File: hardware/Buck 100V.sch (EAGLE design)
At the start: 26 parts, among them M1 SI3430DV, M2 SI5435BDC, Q1 FMMT625, Q2 FMMT723, U1 LT3756EMSE

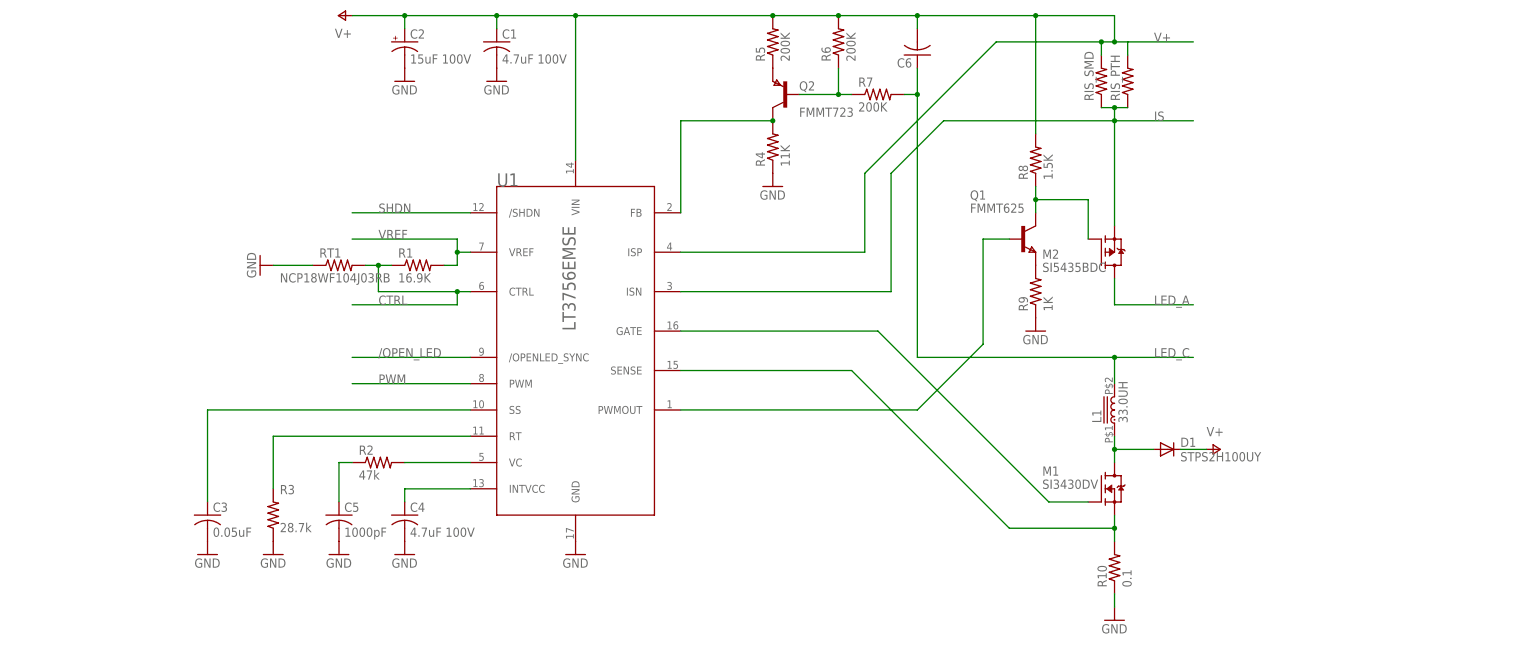
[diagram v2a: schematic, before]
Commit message: Finished schematic (needs a careful double check). Added LTSpice output files to .gitignore.
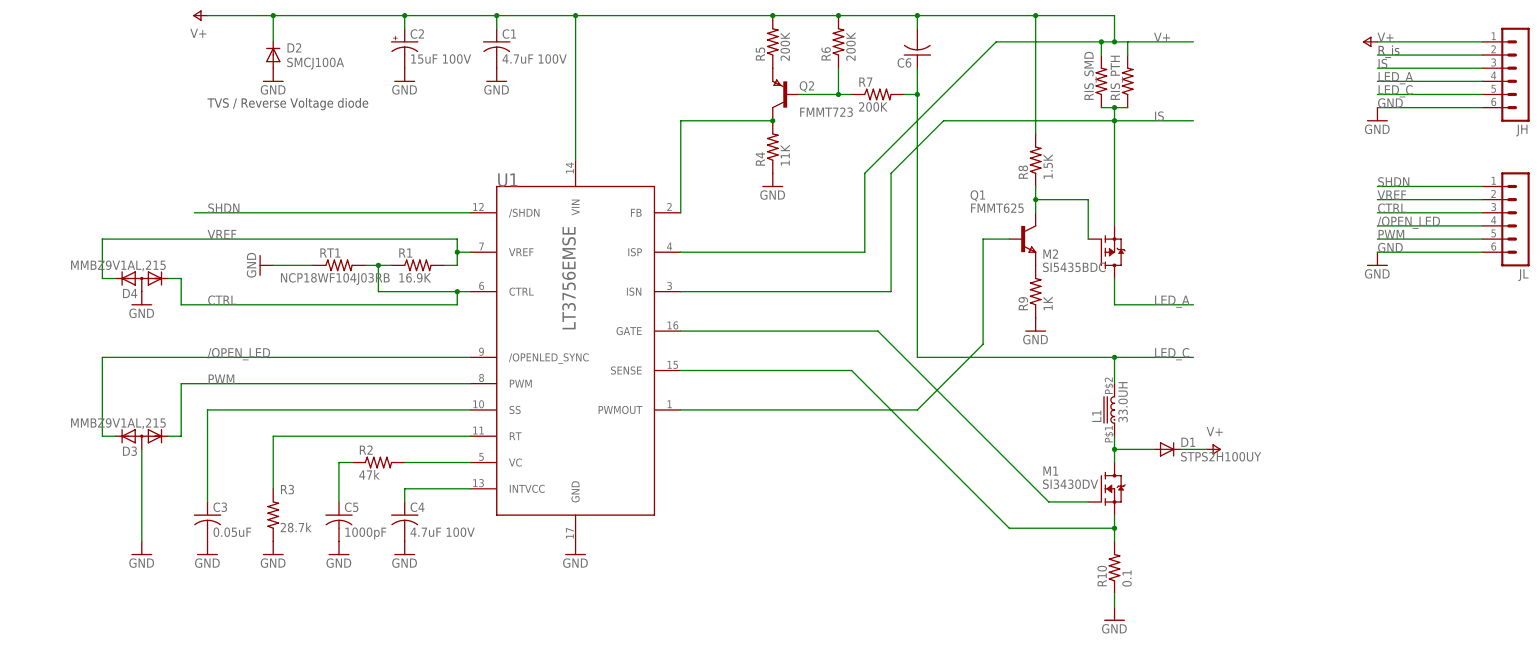
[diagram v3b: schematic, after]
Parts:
- added D2: SMCJ100A, diode:DIODE-SMC
- added D3, D4: MMBZ9V1AL,215, diode:DIODE-2CA|ACSOT23
- added JH, JL: (no value), con-lstb:MA06-1
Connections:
- net /OPEN_LED: now also D3.K2, JL.4
- net CTRL: now also D4.K1, JL.3
- net GND: now also D2.A, D3.A, D4.A, JH.6, JL.6
- net IS: now also JH.3
- net LED_A: now also JH.4
- net LED_C: now also JH.5
- net PWM: now also D3.K1, JL.5
- net SHDN: now also JL.1
- net V+: now also D2.C, JH.1, JH.2
- net VREF: now also D4.K2, JL.2
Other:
- note added: "R_is"
- note added: "TVS / Reverse Voltage diode"
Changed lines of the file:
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@@
 <part name="D1" library="diode" deviceset="DIODE-" device="SMB" value="STPS2H100UY"/>
 <part name="P+2" library="supply1" deviceset="V+" device=""/>
+<part name="D2" library="diode" deviceset="DIODE-" device="SMC" value="SMCJ100A"/>
+<part name="GND12" library="supply1" deviceset="GND" device=""/>
+<part name="D3" library="diode" deviceset="DIODE-2CA|AC" device="SOT23" value="MMBZ9V1AL,215"/>
+<part name="GND13" library="supply1" deviceset="GND" device=""/>
+<part name="D4" library="diode" deviceset="DIODE-2CA|AC" device="SOT23" value="MMBZ9V1AL,215"/>
+<part name="GND14" library="supply1" deviceset="GND" device=""/>
+<part name="P+3" library="supply1" deviceset="V+" device=""/>
+<part name="GND15" library="supply1" deviceset="GND" device=""/>
+<part name="JH" library="con-lstb" deviceset="MA06-1" device=""/>
+<part name="JL" library="con-lstb" deviceset="MA06-1" device=""/>
+<part name="GND16" library="supply1" deviceset="GND" device=""/>
 </parts>
 <sheets>
 <sheet>
 <plain>
+<text x="-71.12" y="45.72" size="1.778" layer="97">TVS / Reverse Voltage diode</text>
+<text x="154.94" y="55.88" size="1.778" layer="97">R_is</text>
 </plain>
 <instances>
@@
 <instance part="GND2" gate="1" x="-33.02" y="50.8"/>
 <instance part="GND3" gate="1" x="-15.24" y="50.8"/>
-<instance part="P+1" gate="1" x="-45.72" y="63.5" rot="R90"/>
+<instance part="P+1" gate="1" x="-73.66" y="63.5" rot="R90"/>
 <instance part="R1" gate="G$1" x="-30.48" y="15.24"/>
 <instance part="RT1" gate="G$1" x="-45.72" y="15.24" smashed="yes">
@@
 <instance part="D1" gate="G$1" x="114.3" y="-20.32"/>
 <instance part="P+2" gate="1" x="124.46" y="-20.32" rot="R270"/>
+<instance part="D2" gate="G$1" x="-58.42" y="55.88" smashed="yes" rot="R90">
+<attribute name="NAME" x="-55.88" y="56.3626" size="1.778" layer="95"/>
+<attribute name="VALUE" x="-55.88" y="53.5686" size="1.778" layer="96"/>
+</instance>
+<instance part="GND12" gate="1" x="-58.42" y="50.8"/>
+<instance part="D3" gate="G$1" x="-83.82" y="-17.78" rot="R180"/>
+<instance part="GND13" gate="1" x="-83.82" y="-40.64"/>
+<instance part="D4" gate="G$1" x="-83.82" y="12.7" rot="R180"/>
+<instance part="GND14" gate="1" x="-83.82" y="7.62"/>
+<instance part="P+3" gate="1" x="152.4" y="58.42" smashed="yes" rot="R90">
+<attribute name="VALUE" x="154.94" y="58.42" size="1.778" layer="96"/>
+</instance>
+<instance part="GND15" gate="1" x="154.94" y="15.24"/>
+<instance part="JH" gate="1" x="182.88" y="50.8" rot="R180"/>
+<instance part="JL" gate="1" x="182.88" y="22.86" rot="R180"/>
+<instance part="GND16" gate="1" x="154.94" y="43.18"/>
 </instances>
 <busses>
@@
 <pinref part="R10" gate="G$1" pin="1"/>
 <wire x1="104.14" y1="-50.8" x2="104.14" y2="-48.26" width="0.1524" layer="91"/>
+</segment>
+<segment>
+<pinref part="D2" gate="G$1" pin="A"/>
+<pinref part="GND12" gate="1" pin="GND"/>
+</segment>
+<segment>
+<pinref part="D3" gate="G$1" pin="A"/>
+<pinref part="GND13" gate="1" pin="GND"/>
+<wire x1="-83.82" y1="-38.1" x2="-83.82" y2="-20.32" width="0.1524" layer="91"/>
+</segment>
+<segment>
+<pinref part="D4" gate="G$1" pin="A"/>
+<pinref part="GND14" gate="1" pin="GND"/>
+</segment>
+<segment>
+<wire x1="175.26" y1="17.78" x2="154.94" y2="17.78" width="0.1524" layer="91"/>
+<label x="154.94" y="17.78" size="1.778" layer="95"/>
+<pinref part="GND15" gate="1" pin="GND"/>
+<pinref part="JL" gate="1" pin="6"/>
+</segment>
+<segment>
+<pinref part="JH" gate="1" pin="6"/>
+<pinref part="GND16" gate="1" pin="GND"/>
+<wire x1="154.94" y1="45.72" x2="175.26" y2="45.72" width="0.1524" layer="91"/>
+<label x="154.94" y="45.72" size="1.778" layer="95"/>
 </segment>
 </net>
@@
 <junction x="-15.24" y="63.5"/>
 <pinref part="P+1" gate="1" pin="V+"/>
-<wire x1="-43.18" y1="63.5" x2="-33.02" y2="63.5" width="0.1524" layer="91"/>
+<wire x1="-71.12" y1="63.5" x2="-58.42" y2="63.5" width="0.1524" layer="91"/>
 <junction x="-33.02" y="63.5"/>
 <pinref part="R6" gate="G$1" pin="2"/>
 <pinref part="R5" gate="G$1" pin="2"/>
+<wire x1="-58.42" y1="63.5" x2="-33.02" y2="63.5" width="0.1524" layer="91"/>
 <wire x1="50.8" y1="63.5" x2="38.1" y2="63.5" width="0.1524" layer="91"/>
 <wire x1="38.1" y1="63.5" x2="0" y2="63.5" width="0.1524" layer="91"/>
@@
 <wire x1="88.9" y1="40.64" x2="88.9" y2="63.5" width="0.1524" layer="91"/>
 <junction x="88.9" y="63.5"/>
+<pinref part="D2" gate="G$1" pin="C"/>
+<wire x1="-58.42" y1="58.42" x2="-58.42" y2="63.5" width="0.1524" layer="91"/>
+<junction x="-58.42" y="63.5"/>
 </segment>
 <segment>
@@
 <wire x1="121.92" y1="-20.32" x2="116.84" y2="-20.32" width="0.1524" layer="91"/>
 </segment>
+<segment>
+<pinref part="P+3" gate="1" pin="V+"/>
+<wire x1="154.94" y1="58.42" x2="175.26" y2="58.42" width="0.1524" layer="91"/>
+<pinref part="JH" gate="1" pin="1"/>
+</segment>
+<segment>
+<wire x1="175.26" y1="55.88" x2="154.94" y2="55.88" width="0.1524" layer="91"/>
+<pinref part="JH" gate="1" pin="2"/>
+</segment>
 </net>
 <net name="SHDN" class="0">
 <segment>
 <pinref part="U1" gate="G$1" pin="/SHDN"/>
-<wire x1="-20.32" y1="25.4" x2="-43.18" y2="25.4" width="0.1524" layer="91"/>
-<label x="-38.1" y="25.4" size="1.778" layer="95"/>
+<wire x1="-20.32" y1="25.4" x2="-73.66" y2="25.4" width="0.1524" layer="91"/>
+<label x="-71.12" y="25.4" size="1.778" layer="95"/>
+</segment>
+<segment>
+<wire x1="175.26" y1="30.48" x2="154.94" y2="30.48" width="0.1524" layer="91"/>
+<label x="154.94" y="30.48" size="1.778" layer="95"/>
+<pinref part="JL" gate="1" pin="1"/>
 </segment>
 </net>
@@
 <wire x1="-22.86" y1="15.24" x2="-25.4" y2="15.24" width="0.1524" layer="91"/>
 <wire x1="-22.86" y1="17.78" x2="-22.86" y2="20.32" width="0.1524" layer="91"/>
-<label x="-38.1" y="20.32" size="1.778" layer="95"/>
+<label x="-71.12" y="20.32" size="1.778" layer="95"/>
 <junction x="-22.86" y="17.78"/>
-<wire x1="-22.86" y1="20.32" x2="-43.18" y2="20.32" width="0.1524" layer="91"/>
+<wire x1="-22.86" y1="20.32" x2="-91.44" y2="20.32" width="0.1524" layer="91"/>
+<pinref part="D4" gate="G$1" pin="K2"/>
+<wire x1="-88.9" y1="12.7" x2="-91.44" y2="12.7" width="0.1524" layer="91"/>
+<wire x1="-91.44" y1="12.7" x2="-91.44" y2="20.32" width="0.1524" layer="91"/>
+</segment>
+<segment>
+<wire x1="175.26" y1="27.94" x2="154.94" y2="27.94" width="0.1524" layer="91"/>
+<label x="154.94" y="27.94" size="1.778" layer="95"/>
+<pinref part="JL" gate="1" pin="2"/>
 </segment>
 </net>
@@
 <wire x1="-20.32" y1="10.16" x2="-22.86" y2="10.16" width="0.1524" layer="91"/>
 <wire x1="-22.86" y1="10.16" x2="-22.86" y2="7.62" width="0.1524" layer="91"/>
-<wire x1="-22.86" y1="7.62" x2="-43.18" y2="7.62" width="0.1524" layer="91"/>
-<label x="-38.1" y="7.62" size="1.778" layer="95"/>
+<wire x1="-22.86" y1="7.62" x2="-76.2" y2="7.62" width="0.1524" layer="91"/>
+<label x="-71.12" y="7.62" size="1.778" layer="95"/>
 <pinref part="R1" gate="G$1" pin="1"/>
 <pinref part="RT1" gate="G$1" pin="2"/>
@@
 <junction x="-22.86" y="10.16"/>
 <junction x="-38.1" y="15.24"/>
+<pinref part="D4" gate="G$1" pin="K1"/>
+<wire x1="-78.74" y1="12.7" x2="-76.2" y2="12.7" width="0.1524" layer="91"/>
+<wire x1="-76.2" y1="12.7" x2="-76.2" y2="7.62" width="0.1524" layer="91"/>
+</segment>
+<segment>
+<wire x1="175.26" y1="25.4" x2="154.94" y2="25.4" width="0.1524" layer="91"/>
+<label x="154.94" y="25.4" size="1.778" layer="95"/>
+<pinref part="JL" gate="1" pin="3"/>
 </segment>
 </net>
@@
 <segment>
 <pinref part="U1" gate="G$1" pin="/OPENLED_SYNC"/>
-<wire x1="-20.32" y1="-2.54" x2="-43.18" y2="-2.54" width="0.1524" layer="91"/>
-<label x="-38.1" y="-2.54" size="1.778" layer="95"/>
+<wire x1="-20.32" y1="-2.54" x2="-91.44" y2="-2.54" width="0.1524" layer="91"/>
+<label x="-71.12" y="-2.54" size="1.778" layer="95"/>
+<pinref part="D3" gate="G$1" pin="K2"/>
+<wire x1="-88.9" y1="-17.78" x2="-91.44" y2="-17.78" width="0.1524" layer="91"/>
+<wire x1="-91.44" y1="-17.78" x2="-91.44" y2="-2.54" width="0.1524" layer="91"/>
+</segment>
+<segment>
+<wire x1="175.26" y1="22.86" x2="154.94" y2="22.86" width="0.1524" layer="91"/>
+<label x="154.94" y="22.86" size="1.778" layer="95"/>
+<pinref part="JL" gate="1" pin="4"/>
 </segment>
 </net>
@@
 <segment>
 <pinref part="U1" gate="G$1" pin="PWM"/>
-<wire x1="-20.32" y1="-7.62" x2="-43.18" y2="-7.62" width="0.1524" layer="91"/>
-<label x="-38.1" y="-7.62" size="1.778" layer="95"/>
+<wire x1="-20.32" y1="-7.62" x2="-76.2" y2="-7.62" width="0.1524" layer="91"/>
+<label x="-71.12" y="-7.62" size="1.778" layer="95"/>
+<pinref part="D3" gate="G$1" pin="K1"/>
+<wire x1="-78.74" y1="-17.78" x2="-76.2" y2="-17.78" width="0.1524" layer="91"/>
+<wire x1="-76.2" y1="-17.78" x2="-76.2" y2="-7.62" width="0.1524" layer="91"/>
+</segment>
+<segment>
+<pinref part="JL" gate="1" pin="5"/>
+<wire x1="175.26" y1="20.32" x2="154.94" y2="20.32" width="0.1524" layer="91"/>
+<label x="154.94" y="20.32" size="1.778" layer="95"/>
 </segment>
 </net>
@@
 <label x="111.76" y="43.18" size="1.778" layer="95"/>
 </segment>
+<segment>
+<wire x1="175.26" y1="53.34" x2="154.94" y2="53.34" width="0.1524" layer="91"/>
+<label x="154.94" y="53.34" size="1.778" layer="95"/>
+<pinref part="JH" gate="1" pin="3"/>
+</segment>
 </net>
 <net name="LED_A" class="0">
@@
 <wire x1="104.14" y1="7.62" x2="119.38" y2="7.62" width="0.1524" layer="91"/>
 <label x="111.76" y="7.62" size="1.778" layer="95"/>
+</segment>
+<segment>
+<wire x1="175.26" y1="50.8" x2="154.94" y2="50.8" width="0.1524" layer="91"/>
+<label x="154.94" y="50.8" size="1.778" layer="95"/>
+<pinref part="JH" gate="1" pin="4"/>
 </segment>
 </net>
@@
 <junction x="66.04" y="48.26"/>
 </segment>
-</net>
+<segment>
+<wire x1="154.94" y1="48.26" x2="175.26" y2="48.26" width="0.1524" layer="91"/>
+<label x="154.94" y="48.26" size="1.778" layer="95"/>
+<pinref part="JH" gate="1" pin="5"/>
+</segment>
+</net>

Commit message: Beautify and correct the schematic. Made the two headers different sizes so that it is harder to put the part in backwards. Next step is to run and confirm BOM.
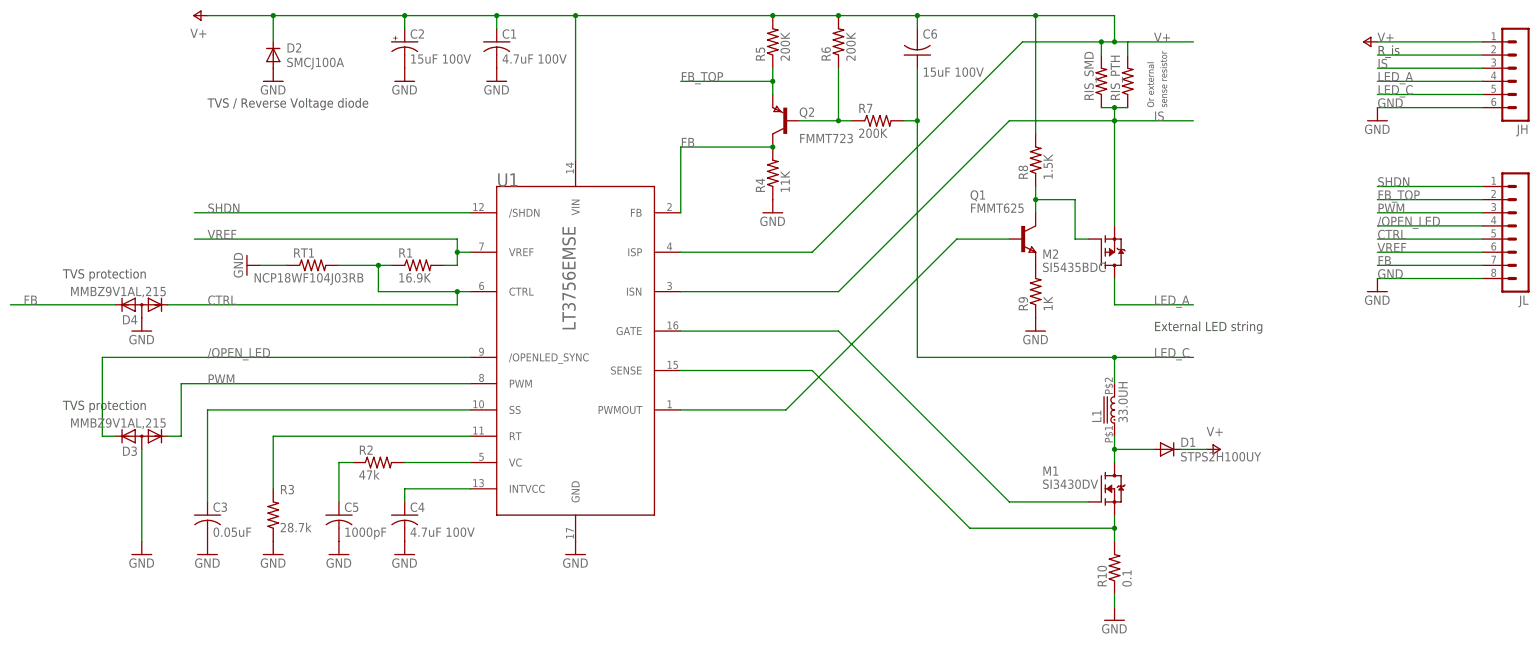
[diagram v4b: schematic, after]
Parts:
- C6: value (none) -> 15uF 100V
- JL: device con-lstb:MA06-1 -> con-lstb:MA08-1
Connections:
- removed net N$6: Q2.C, R4.2, U1.FB
- removed net N$7: Q2.E, R5.1
- new net FB: D4.K2, JL.7, Q2.C, R4.2, U1.FB
- new net FB_TOP: JL.2, Q2.E, R5.1
- net CTRL: now also JL.5; no longer JL.3
- net GND: now also JL.8; no longer JL.6
- net PWM: now also JL.3; no longer JL.5
- net VREF: now also JL.6; no longer D4.K2, JL.2
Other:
- note added: "External LED string"
- note added: "Or external"
- note added: "TVS protection"
- note added: "sense resistor"
- moved on the sheet: D4, Q2, R4, R7, RT1

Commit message: Minor fixes.
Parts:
- C3: value 0.05uF -> 0.047uF
- C6: device rcl:C-USC2220K -> rcl:CPOL-USE2,5-6E
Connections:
- net LED_C: now also C6.+; no longer C6.1
- net V+: now also C6.-; no longer C6.2
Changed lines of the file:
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@@
 <part name="RT1" library="rcl" deviceset="R-US_" device="R0805" value="NCP18WF104J03RB"/>
 <part name="GND4" library="supply1" deviceset="GND" device=""/>
-<part name="C3" library="rcl" deviceset="C-US" device="C0805" value="0.05uF"/>
+<part name="C3" library="rcl" deviceset="C-US" device="C0805" value="0.047uF"/>
 <part name="C4" library="rcl" deviceset="C-US" device="C0805" value="4.7uF 100V"/>
 <part name="C5" library="rcl" deviceset="C-US" device="C0805" value="1000pF"/>
@@
 <part name="L1" library="LED-drivers" deviceset="ASPI-0612FS" device="" value="33.0UH"/>
 <part name="M2" library="LED-drivers" deviceset="SI5435BDC" device=""/>
-<part name="C6" library="rcl" deviceset="C-US" device="C2220K" value="15uF 100V"/>
 <part name="Q1" library="zetex" deviceset="FMMT6*" device="" technology="25"/>
 <part name="R8" library="rcl" deviceset="R-US_" device="R0805" value="1.5K"/>
@@
 <part name="JH" library="con-lstb" deviceset="MA06-1" device=""/>
 <part name="JL" library="con-lstb" deviceset="MA08-1" device=""/>
+<part name="C6" library="rcl" deviceset="CPOL-US" device="E2,5-6E" value="15uF 100V"/>
 </parts>
 <sheets>
@@
 <instance part="L1" gate="G$1" x="104.14" y="-12.7" rot="R90"/>
 <instance part="M2" gate="G$1" x="101.6" y="17.78"/>
-<instance part="C6" gate="G$1" x="66.04" y="55.88" smashed="yes" rot="R180">
-<attribute name="NAME" x="67.056" y="59.055" size="1.778" layer="95"/>
-<attribute name="VALUE" x="67.056" y="51.689" size="1.778" layer="96"/>
-</instance>
 <instance part="Q1" gate="G$1" x="86.36" y="20.32"/>
 <instance part="R8" gate="G$1" x="88.9" y="35.56" rot="R90"/>
@@
 <instance part="JH" gate="1" x="182.88" y="50.8" rot="R180"/>
 <instance part="JL" gate="1" x="182.88" y="22.86" rot="R180"/>
+<instance part="C6" gate="G$1" x="66.04" y="55.88" smashed="yes" rot="R180">
+<attribute name="NAME" x="69.596" y="59.055" size="1.778" layer="95"/>
+<attribute name="VALUE" x="69.596" y="54.229" size="1.778" layer="96"/>
+</instance>
 </instances>
 <busses>
@@
 <wire x1="66.04" y1="63.5" x2="50.8" y2="63.5" width="0.1524" layer="91"/>
 <junction x="50.8" y="63.5"/>
-<pinref part="C6" gate="G$1" pin="2"/>
 <wire x1="66.04" y1="60.96" x2="66.04" y2="63.5" width="0.1524" layer="91"/>
 <junction x="66.04" y="63.5"/>
@@
 <wire x1="-58.42" y1="58.42" x2="-58.42" y2="63.5" width="0.1524" layer="91"/>
 <junction x="-58.42" y="63.5"/>
+<pinref part="C6" gate="G$1" pin="-"/>
 </segment>
 <segment>
@@
 <wire x1="66.04" y1="43.18" x2="63.5" y2="43.18" width="0.1524" layer="91"/>
 <junction x="104.14" y="-2.54"/>
-<pinref part="C6" gate="G$1" pin="1"/>
 <wire x1="66.04" y1="53.34" x2="66.04" y2="43.18" width="0.1524" layer="91"/>
 <junction x="66.04" y="43.18"/>
-</segment>
-<segment>
+<pinref part="C6" gate="G$1" pin="+"/>
+</segment>
+<segment>
